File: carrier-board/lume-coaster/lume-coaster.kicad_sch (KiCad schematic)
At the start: 0 parts

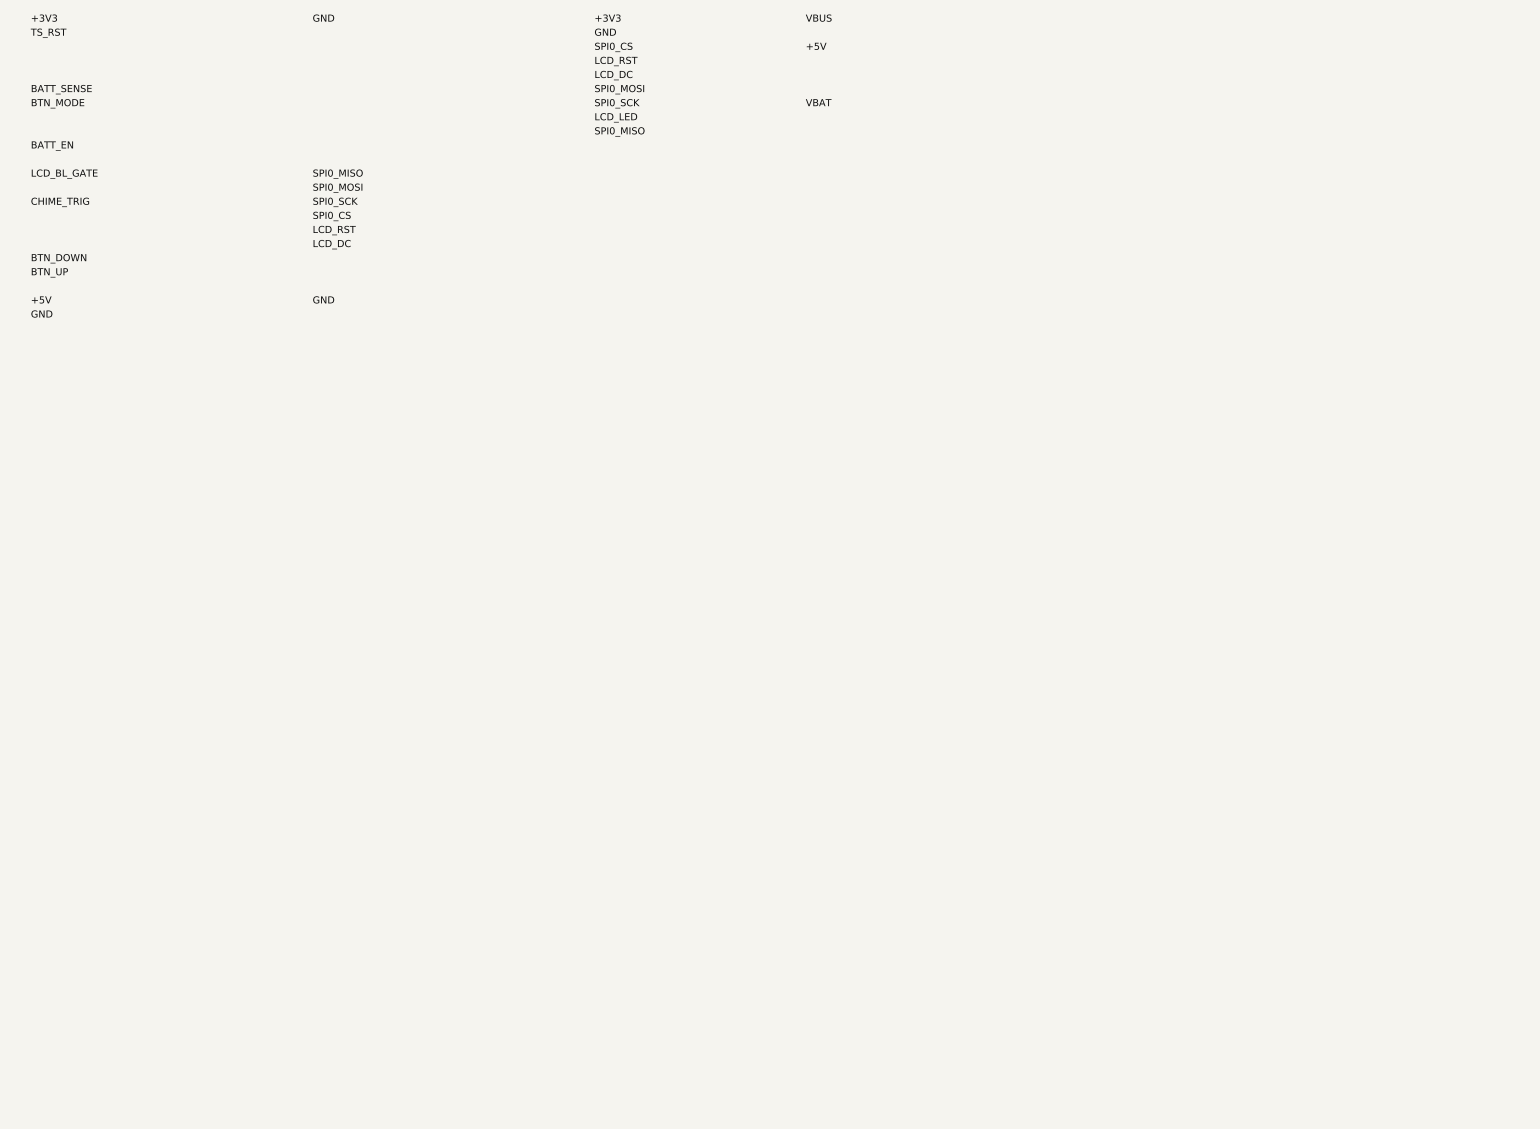
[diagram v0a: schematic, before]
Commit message: feat(week1): lume-coaster carrier board - fab-ready
- Tuya T5AI-Core (T5-E1) carrier, 85x40mm 2-layer
- 2x1x22 PinSocket headers, 25.4mm center-to-center
- Full GND pour on B.Cu with on-disk filled polygon
- ERC 0/0/0, DRC 0 violations / 0 unconnected / 0 footprint errors
- Gerbers + drill archive verified (G36/G37 solid copper fill present)
- Untrack .history submodule, KiCad lockfiles, scratch generators
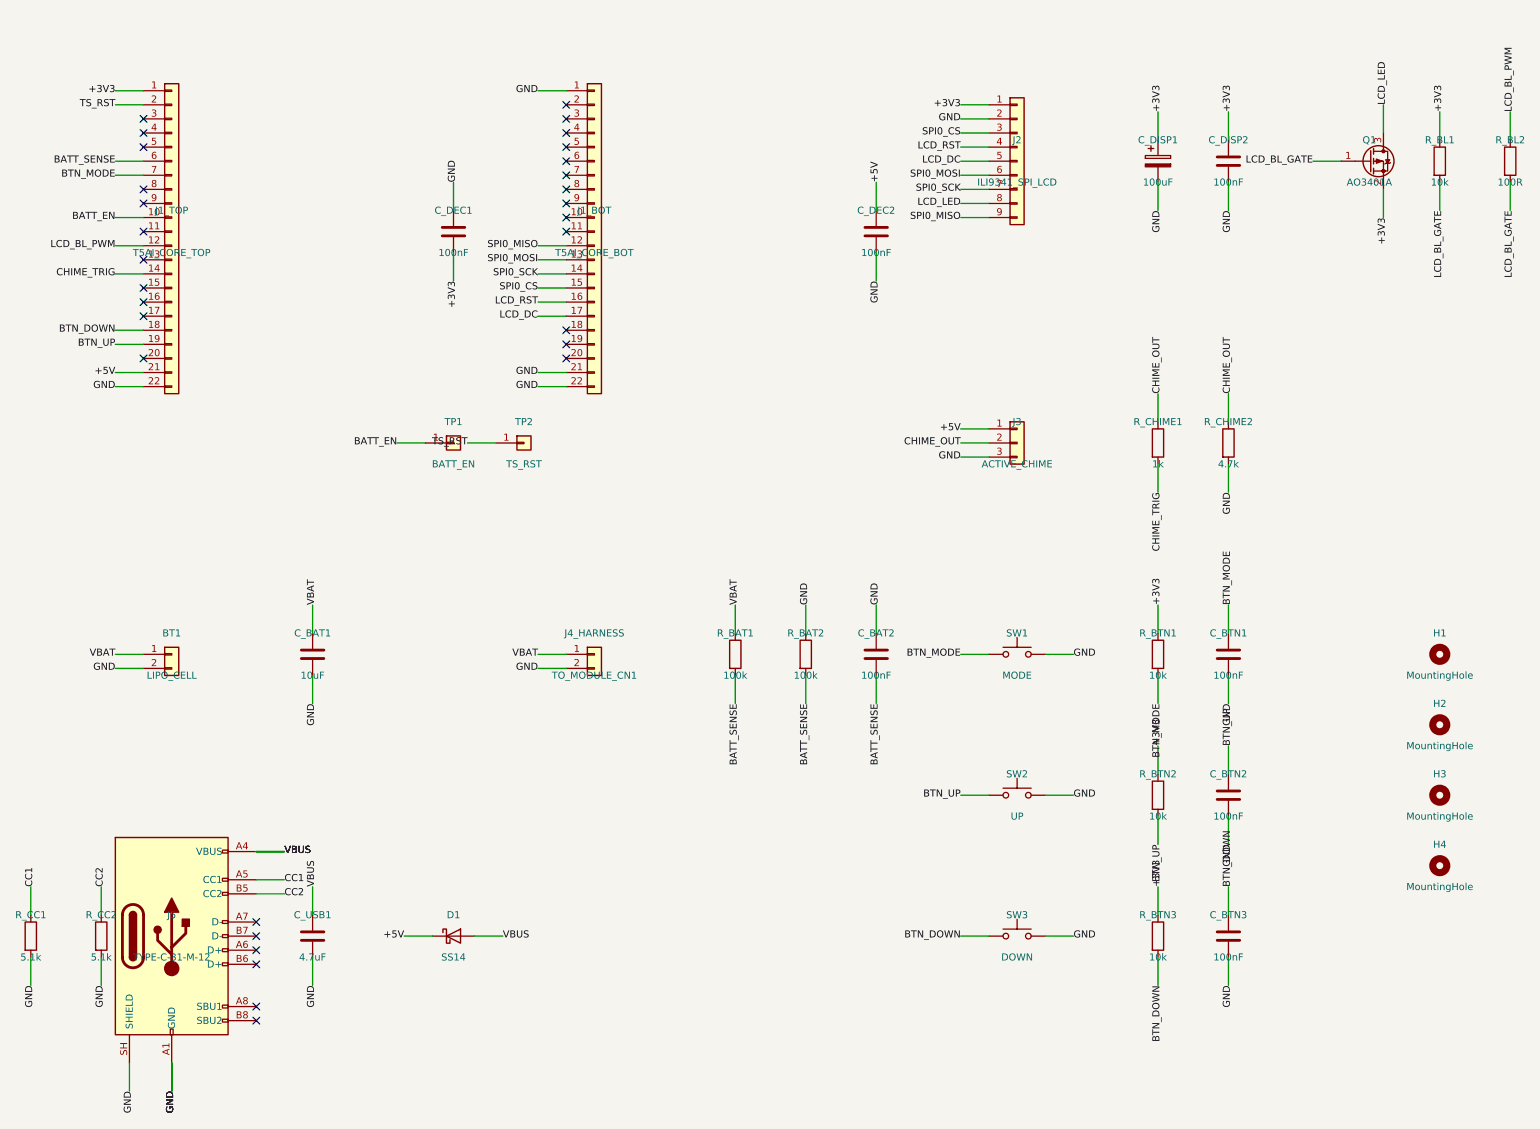
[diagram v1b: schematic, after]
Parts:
- added BT1: LIPO_CELL, Connector_JST:JST_PH_S2B-PH-K_1x02_P2.00mm_Horizontal, symbol Connector_Generic:Conn_01x02
- added C_BAT1: 10uF, Capacitor_SMD:C_0805_2012Metric, symbol Device:C
- added C_BAT2, C_BTN1, C_BTN2, C_BTN3, C_DEC1, C_DEC2, C_DISP2: 100nF, Capacitor_SMD:C_0805_2012Metric, symbol Device:C
- added C_DISP1: 100uF, Capacitor_SMD:CP_Elec_6.3x5.4, symbol Device:C_Polarized
- added C_USB1: 4.7uF, Capacitor_SMD:C_0805_2012Metric, symbol Device:C
- added D1: SS14, Diode_SMD:D_SMA, symbol Device:D_Schottky
- added H1, H2, H3, H4: MountingHole, MountingHole:MountingHole_3.2mm_M3, symbol Mechanical:MountingHole
- added J1_BOT: T5AI_CORE_BOT, Connector_PinSocket_2.54mm:PinSocket_1x22_P2.54mm_Vertical, symbol Connector_Generic:Conn_01x22
- added J1_TOP: T5AI_CORE_TOP, Connector_PinSocket_2.54mm:PinSocket_1x22_P2.54mm_Vertical, symbol Connector_Generic:Conn_01x22
- added J2: ILI9341_SPI_LCD, Connector_PinHeader_2.54mm:PinHeader_1x09_P2.54mm_Vertical, symbol Connector_Generic:Conn_01x09
- added J3: ACTIVE_CHIME, Connector_PinHeader_2.54mm:PinHeader_1x03_P2.54mm_Horizontal, symbol Connector_Generic:Conn_01x03
- added J4_HARNESS: TO_MODULE_CN1, Connector_JST:JST_GH_SM02B-GHS-TB_1x02-1MP_P1.25mm_Horizontal, symbol Connector_Generic:Conn_01x02
- added J5: TYPE-C-31-M-12, Connector_USB:USB_C_Receptacle_HRO_TYPE-C-31-M-12, symbol Connector:USB_C_Receptacle_USB2.0_16P
- added Q1: AO3401A, Package_TO_SOT_SMD:SOT-23, symbol Transistor_FET:TP0610T
- added R_BAT1, R_BAT2: 100k, Resistor_SMD:R_0805_2012Metric, symbol Device:R
- added R_BL1, R_BTN1, R_BTN2, R_BTN3: 10k, Resistor_SMD:R_0805_2012Metric, symbol Device:R
- added R_BL2: 100R, Resistor_SMD:R_0805_2012Metric, symbol Device:R
- added R_CC1, R_CC2: 5.1k, Resistor_SMD:R_0805_2012Metric, symbol Device:R
- added R_CHIME1: 1k, Resistor_SMD:R_0805_2012Metric, symbol Device:R
- added R_CHIME2: 4.7k, Resistor_SMD:R_0805_2012Metric, symbol Device:R
- added SW1: MODE, Button_Switch_SMD:SW_Push_1TS009xxxx-xxxx-xxxx_6x6x5mm, symbol Switch:SW_Push
- added SW2: UP, Button_Switch_SMD:SW_Push_1TS009xxxx-xxxx-xxxx_6x6x5mm, symbol Switch:SW_Push
- added SW3: DOWN, Button_Switch_SMD:SW_Push_1TS009xxxx-xxxx-xxxx_6x6x5mm, symbol Switch:SW_Push
- added TP1: BATT_EN, TestPoint:TestPoint_Pad_D1.0mm, symbol Connector_Generic:Conn_01x01
- added TP2: TS_RST, TestPoint:TestPoint_Pad_D1.0mm, symbol Connector_Generic:Conn_01x01
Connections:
- net +3V3: now also C_DEC1.2, C_DISP1.1, C_DISP2.1, J1_TOP.1 (Pin_1), J2.1 (Pin_1), Q1.2 (S), R_BL1.1, R_BTN1.1, R_BTN2.1, R_BTN3.1
- net +5V: now also C_DEC2.1, D1.1 (K), J1_TOP.21 (Pin_21), J3.1 (Pin_1)
- net BATT_EN: now also J1_TOP.10 (Pin_10), TP1.1 (Pin_1)
- net BATT_SENSE: now also C_BAT2.2, J1_TOP.6 (Pin_6), R_BAT1.2, R_BAT2.2
- net BTN_DOWN: now also C_BTN3.1, J1_TOP.18 (Pin_18), R_BTN3.2, SW3.1
- net BTN_MODE: now also C_BTN1.1, J1_TOP.7 (Pin_7), R_BTN1.2, SW1.1
- net BTN_UP: now also C_BTN2.1, J1_TOP.19 (Pin_19), R_BTN2.2, SW2.1
- net CHIME_TRIG: now also J1_TOP.14 (Pin_14), R_CHIME1.2
- net GND: now also BT1.2 (Pin_2), C_BAT1.2, C_BAT2.1, C_BTN1.2, C_BTN2.2, C_BTN3.2, C_DEC1.1, C_DEC2.2, C_DISP1.2, C_DISP2.2, C_USB1.2, J1_BOT.1 (Pin_1), J1_BOT.21 (Pin_21), J1_BOT.22 (Pin_22), J1_TOP.22 (Pin_22), J2.2 (Pin_2), J3.3 (Pin_3), J4_HARNESS.2 (Pin_2), J5.A1 (GND), J5.A12 (GND), J5.B1 (GND), J5.B12 (GND), J5.SH (SHIELD), R_BAT2.1, R_CC1.2, R_CC2.2, R_CHIME2.2, SW1.2, SW2.2, SW3.2
- net LCD_BL_GATE: now also Q1.1 (G), R_BL1.2, R_BL2.2
- net LCD_DC: now also J1_BOT.17 (Pin_17), J2.5 (Pin_5)
- net LCD_LED: now also J2.8 (Pin_8), Q1.3 (D)
- net LCD_RST: now also J1_BOT.16 (Pin_16), J2.4 (Pin_4)
- net SPI0_CS: now also J1_BOT.15 (Pin_15), J2.3 (Pin_3)
- net SPI0_MISO: now also J1_BOT.12 (Pin_12), J2.9 (Pin_9)
- net SPI0_MOSI: now also J1_BOT.13 (Pin_13), J2.6 (Pin_6)
- net SPI0_SCK: now also J1_BOT.14 (Pin_14), J2.7 (Pin_7)
- net TS_RST: now also J1_TOP.2 (Pin_2), TP2.1 (Pin_1)
- net VBAT: now also BT1.1 (Pin_1), C_BAT1.1, J4_HARNESS.1 (Pin_1), R_BAT1.1
- net VBUS: now also C_USB1.1, D1.2 (A), J5.A4 (VBUS), J5.A9 (VBUS), J5.B4 (VBUS), J5.B9 (VBUS)
- new net CC1: J5.A5 (CC1), R_CC1.1
- new net CC2: J5.B5 (CC2), R_CC2.1
- new net CHIME_OUT: J3.2 (Pin_2), R_CHIME1.1, R_CHIME2.1
- new net LCD_BL_PWM: J1_TOP.12 (Pin_12), R_BL2.1
- no-connect marks 0 -> 30
